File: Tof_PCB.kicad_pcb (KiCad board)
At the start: 2 copper layers, 110.3 x 64.3 mm, 203 parts, among them IC1 NC7WZ00K8X, J1 Screw_Terminal_01x02, J2 Screw_Terminal_01x02, J3 Screw_Terminal_01x02, J4 Conn_02x03_Odd_Even, J5 Conn_01x04, J6 Conn_01x04, M1 mounting_holes_laser, M2 mounting_holes_laser, M3 mounting_holes_laser, M4 mounting_holes_laser, SW1 SW_Push, U1 ATmega328PB-MU, U10 NC7WZ00K8X, U11 UMCC_50Ohm, U12 UMCC_50Ohm, U13 NC7WZ00K8X, U14 NCP81074BDR2G, U15 LMH6559MF, U16 SiPM-MicroRB, U17 UMCC_50Ohm, U18 ts5a4596, U19 ts5a4596, U2 DAC128S085, U20 MAX40658, U21 LP5907MFX-3.3_NOPB, U22 UMCC_50Ohm, U23 TLV3501, U24 TLV3501, U25 HMC589AST89E, U26 UMCC_50Ohm, U27 UMCC_50Ohm, U28 UMCC_50Ohm, U29 UMCC_50Ohm, U3 LM4132BMF, U4 UMCC_50Ohm, U5 UMCC_50Ohm, U6 HMC589AST89E, U7 TLV3501, U8 UMCC_50Ohm, U9 NC7WZ00K8X, Y1 Crystal_GND24

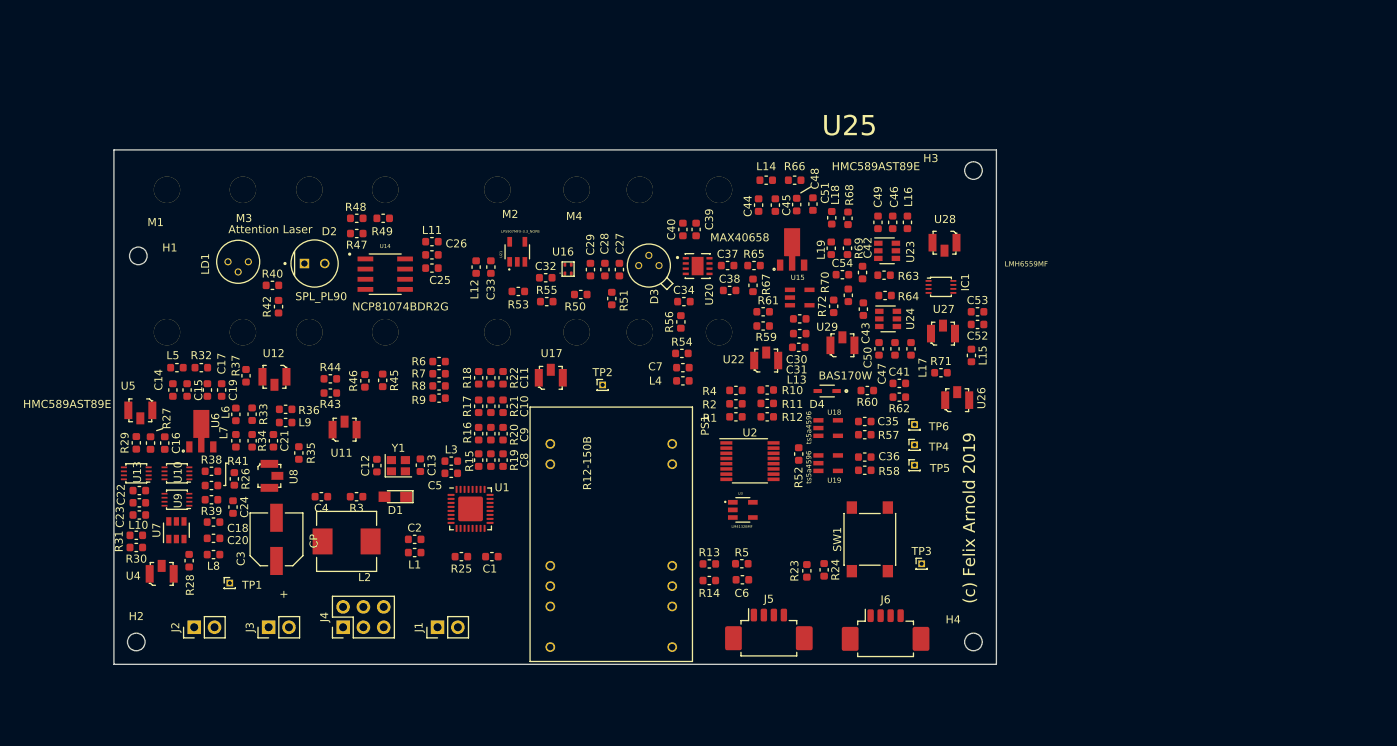
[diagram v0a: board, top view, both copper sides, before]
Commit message: Added RLC values
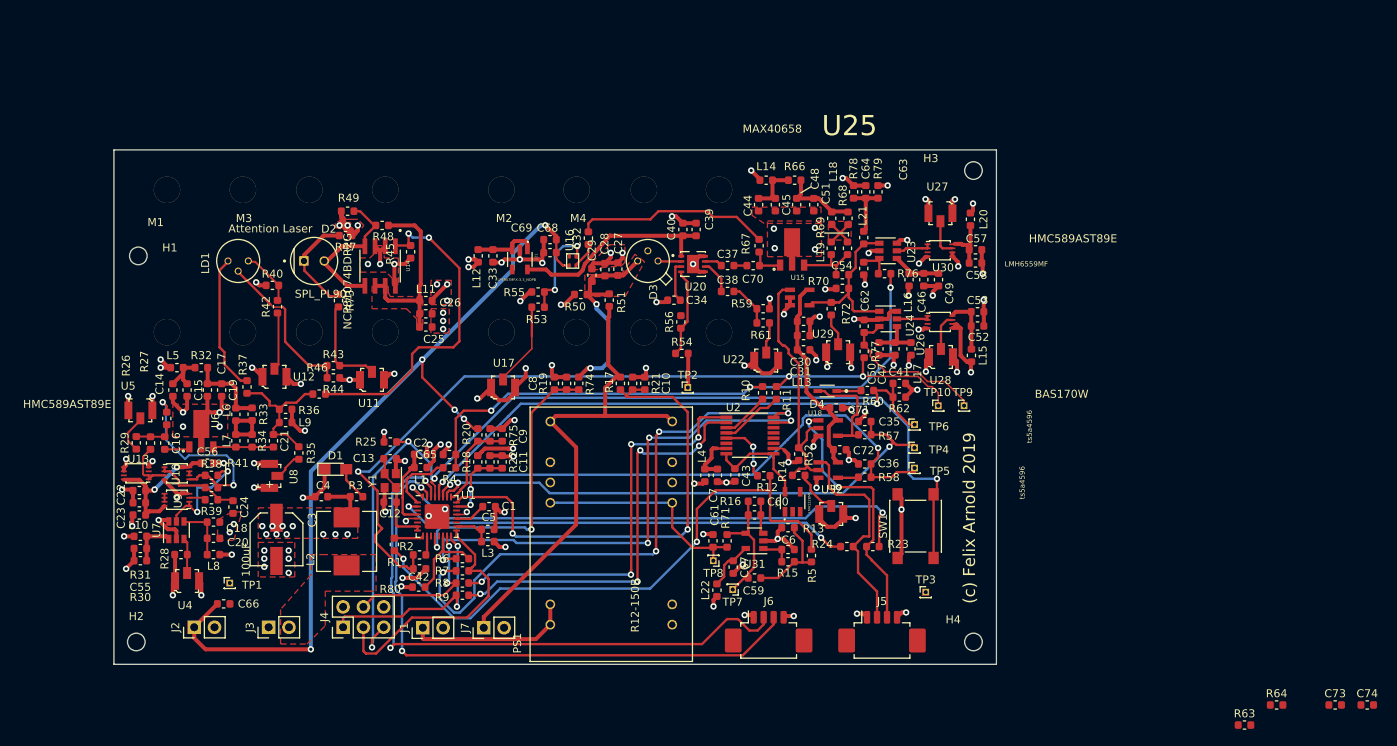
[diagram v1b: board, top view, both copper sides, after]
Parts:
- removed R65: R, Resistor_SMD:R_0603_1608Metric
- added C55: C, Capacitor_SMD:C_0603_1608Metric, F.Cu at (63.0, 99.8)
- added C56: C, Capacitor_SMD:C_0603_1608Metric, F.Cu at (71.4, 89.2)
- added C57: C, Capacitor_SMD:C_0603_1608Metric, F.Cu at (167.4, 62.5)
- added C58: C, Capacitor_SMD:C_0603_1608Metric, F.Cu at (167.4, 64.1)
- added C59: 100nF, Capacitor_SMD:C_0603_1608Metric, F.Cu at (139.8, 103.5)
- added C60: 10nF, Capacitor_SMD:C_0603_1608Metric, F.Cu at (139.8, 95.6)
- added C61: 100nF, Capacitor_SMD:C_0603_1608Metric, F.Cu at (134.6, 98.9)
- added C62: 100nF, Capacitor_SMD:C_0603_1608Metric, F.Cu at (153.5, 72.0)
- added C63: 100nF, Capacitor_SMD:C_0603_1608Metric, F.Cu at (153.4, 64.8)
- added C64: C, Capacitor_SMD:C_0603_1608Metric, F.Cu at (153.7, 55.2)
- added C65: 2.2uF, Capacitor_SMD:C_0603_1608Metric, F.Cu at (101.6, 88.1)
- added C66: 2.2uF, Capacitor_SMD:C_0603_1608Metric, F.Cu at (73.4, 106.7)
- added C67: 100nF, Capacitor_SMD:C_0603_1608Metric, F.Cu at (137.1, 102.1)
- added C68: 2.2uF, Capacitor_SMD:C_0603_1608Metric, F.Cu at (114.2, 61.2)
- added C69: 100nF, Capacitor_SMD:C_0603_1608Metric, F.Cu at (114.2, 62.8)
- added C70: C, Capacitor_SMD:C_0603_1608Metric, F.Cu at (139.6, 64.5)
- added C71: 2.2uF, Capacitor_SMD:C_0603_1608Metric, F.Cu at (150.0, 82.2)
- added C72: 100nF, Capacitor_SMD:C_0603_1608Metric, F.Cu at (150.4, 87.5)
- added C73: 2.2uF, Capacitor_SMD:C_0603_1608Metric, F.Cu at (212.3, 119.4)
- added C74: 2.2uF, Capacitor_SMD:C_0603_1608Metric, F.Cu at (216.4, 119.4)
- added J7: Screw_Terminal_01x02, IODA_Lib:ScrewTerminal_1x02_P2.54mm_Vertical, F.Cu at (105.9, 109.7)
- added L20: L, Inductor_SMD:L_0603_1608Metric, F.Cu at (166.8, 58.7)
- added L21: L, Inductor_SMD:L_0603_1608Metric, F.Cu at (153.4, 61.0)
- added L22: L, Inductor_SMD:L_0603_1608Metric, F.Cu at (135.1, 105.0)
- added R73: R, Resistor_SMD:R_0603_1608Metric, F.Cu at (87.8, 68.8)
- added R74: 1M, Resistor_SMD:R_0603_1608Metric, F.Cu at (117.8, 79.2)
- added R75: 100k, Resistor_SMD:R_0603_1608Metric, F.Cu at (105.2, 85.6)
- added R76: 50k, Resistor_SMD:R_0603_1608Metric, F.Cu at (156.0, 65.5)
- added R77: 50k, Resistor_SMD:R_0603_1608Metric, F.Cu at (153.5, 75.2)
- added R78: R, Resistor_SMD:R_0603_1608Metric, F.Cu at (152.1, 55.2)
- added R79: R, Resistor_SMD:R_0603_1608Metric, F.Cu at (155.2, 55.2)
- added R80: 20k, Resistor_SMD:R_0603_1608Metric, F.Cu at (97.8, 104.6)
- added TP10: TestPoint, Connector_PinHeader_1.00mm:PinHeader_1x01_P1.00mm_Vertical, F.Cu at (162.7, 82.0)
- added TP7: TestPoint, Connector_PinHeader_1.00mm:PinHeader_1x01_P1.00mm_Vertical, F.Cu at (137.0, 105.0)
- added TP8: TestPoint, Connector_PinHeader_1.00mm:PinHeader_1x01_P1.00mm_Vertical, F.Cu at (134.6, 101.3)
- added TP9: TestPoint, Connector_PinHeader_1.00mm:PinHeader_1x01_P1.00mm_Vertical, F.Cu at (166.0, 82.0)
- added U31: LM321, Package_TO_SOT_SMD:SOT-23-5, F.Cu at (139.8, 98.9)
- added U32: UMCC_50Ohm, IODA_Lib:Molex_734120114_UMC_RF_CONN_Vertical, F.Cu at (149.4, 95.5)
- C1, C2, C5, C7: value 100n -> 100nF
- C10, C11, C27, C31, C32, C33, C37, C38, C39, C4, C42, C8, C9: value C -> 2.2uF
- C12, C13: value C -> 16pF
- C28, C29, C30, C40, C43, C6: value C -> 100nF
- C3: value CP -> 100uF
- C34: value C -> 1uF
- L2: value L -> 6.6u
- R1, R10, R11, R12, R23, R24, R50, R6, R7, R8, R9: value R -> 0R
- R13: value R -> 2k
- R14, R55, R61: value R -> 200R
- R15, R18, R19, R20, R21, R22, R5, R54, R56, R71: value R -> 10k
- R16: value R -> 10R
- R17, R51: value R -> 1M
- R2, R4: value R -> 2.2k
- R25: value R -> 20k
- R52, R53: value R -> 50R
- R59, R63: value R -> 75R
- R64: value R -> 150R
- U26: value UMCC_50Ohm -> NC7WZ00K8X; footprint IODA_Lib:Molex_734120114_UMC_RF_CONN_Vertical -> IODA_Lib:VSSOP-8_2.4x2.1mm_P0.5mm
- moved R63 72.1 mm to (201.0, 121.9)
- moved R64 70.8 mm to (205.0, 119.4)
- moved C42 66.6 mm to (97.9, 102.4), turned to 0 degrees
- moved R1 45.6 mm to (94.7, 99.3), turned to 90 degrees
- moved R2 43.8 mm to (97.9, 100.6), turned to 0 degrees
- moved R15 40.7 mm to (144.0, 101.5), turned to 0 degrees
- moved R4 37.1 mm to (101.6, 89.7)
- moved R16 35.5 mm to (139.8, 93.9), turned to 0 degrees
- moved R71 34.0 mm to (136.3, 98.9), turned to 90 degrees
- moved C43 26.2 mm to (137.3, 90.6), turned to 270 degrees
- moved R6 24.8 mm to (103.3, 101.1)
- moved R7 24.8 mm to (103.3, 102.6)
- moved R8 24.8 mm to (103.3, 104.1)
- moved R9 24.8 mm to (103.3, 105.7)
- moved C10 17.9 mm to (126.0, 79.2)
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- renumbered IC1 to U30
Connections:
- net Net-(C25-Pad1) renamed /Tof Tx/ld_driver_supply
- net Net-(R43-Pad1) renamed /Tof Tx/LD_sense
- C42 pad 1: Net-(C42-Pad1) -> /comp_level_2
- C6 pad 1: /V_adj_apd_filt -> GND
- C6 pad 2: GND -> Net-(C6-Pad2)
- J3 pad 1: /5V_in -> GND
- J3 pad 2: GND -> /5V_in
- J5 pad 2: /lockin_2_mc -> /lockin_2
- J5 pad 3: /lockin_1_mc -> /lockin_1
- PS1 pad 17: Net-(PS1-Pad17) -> /V_adj_apd_filt
- PS1 pad 8: Net-(PS1-Pad17) -> /V_adj_apd_filt
- R13 pad 2: Net-(PS1-Pad17) -> Net-(C59-Pad2)
- R14 pad 1: /V_adj_apd_filt -> Net-(R14-Pad1)
- R14 pad 2: Net-(PS1-Pad17) -> Net-(R14-Pad2)
- R15 pad 1: /V_APD_R_SENS -> Net-(C6-Pad2)
- R15 pad 2: /V_APD_R -> Net-(C59-Pad2)
- R16 pad 1: /V_SiPM_SENSE -> Net-(C59-Pad1)
- R16 pad 2: /V_SiPM -> Net-(C60-Pad2)
- R45 pad 2: /Tof Tx/tx_amp_out -> /Tof Tx/ld_driver_in
- R46 pad 1: Net-(R46-Pad1) -> /Tof Tx/tx_amp_out
- R46 pad 2: /Tof Tx/tx_amp_out -> /Tof Tx/ld_driver_in
- R5 pad 1: /V_adj_apd_filt -> Net-(C59-Pad2)
- R52 pad 2: Net-(R52-Pad2) -> Net-(R14-Pad1)
- R63 pad 1: Net-(C42-Pad1) -> Net-(C38-Pad2)
- R63 pad 2: /comp_level_1 -> GND
- R64 pad 1: Net-(C43-Pad1) -> /Tof Rx/TIA_out
- R64 pad 2: /comp_level_2 -> GND
- R71 pad 1: /Tof Rx/rfamp_out -> /V_adj_apd_filt
- R71 pad 2: Net-(R71-Pad2) -> Net-(C59-Pad1)
- U14 pad 1: Net-(R46-Pad1) -> /Tof Tx/ld_driver_in
- U15 pad 1: Net-(R52-Pad2) -> Net-(R14-Pad1)
- U18 pad 2: Net-(R52-Pad2) -> Net-(R14-Pad1)
- U19 pad 2: Net-(R52-Pad2) -> Net-(R14-Pad1)
- U2 pad 8: Net-(U2-Pad8) -> Net-(C43-Pad1)
- U2 pad 9: Net-(U2-Pad8) -> Net-(C43-Pad1)
- U23 pad 3: Net-(C42-Pad1) -> Net-(C63-Pad1)
- U24 pad 3: Net-(C43-Pad1) -> Net-(C62-Pad1)
- U24 pad 5: Net-(IC1-Pad5) -> Net-(U24-Pad5)
- U26 pad 1: GND -> Net-(U24-Pad5)
- U26 pad 2: Net-(R71-Pad2) -> Net-(U24-Pad5)
- U26 pad 3: GND -> Net-(U26-Pad3)
- U28 pad 2: Net-(IC1-Pad3) -> Net-(U26-Pad7)
- U3 pad 5: Net-(U2-Pad8) -> Net-(C43-Pad1)
- U30 pad 3: Net-(IC1-Pad3) -> Net-(U30-Pad3)
- U30 pad 5: Net-(IC1-Pad5) -> +5V
- U30 pad 6: Net-(IC1-Pad5) -> +5V
- U30 pad 8: Net-(C52-Pad1) -> Net-(C57-Pad1)
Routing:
- net GND: track 0.00 -> 265.8 mm, vias 0 -> 108
- net /~reset: track 0.00 -> 126.4 mm, vias 0 -> 4
- net /V_SiPM: track 0.00 -> 104.7 mm, vias 0 -> 5
- net /comp_level_2: track 0.00 -> 102.7 mm, vias 0 -> 3
- net /RXD: track 0.00 -> 77.1 mm, vias 0 -> 2
- net /comp_level_1: track 0.00 -> 75.6 mm, vias 0 -> 3
- net /TXD: track 0.00 -> 74.7 mm, vias 0 -> 2
- net /V_adj_apd: track 0.00 -> 73.4 mm, vias 0 -> 2
- net /lockin_1_peak: track 0.00 -> 71.7 mm, vias 0 -> 2
- net /lockin_2_filt: track 0.00 -> 71.7 mm, vias 0 -> 2
- net Net-(R7-Pad1): track 0.00 -> 71.6 mm, vias 0 -> 4
- net /lockin_1_filt: track 0.00 -> 68.4 mm, vias 0 -> 2
- net /lockin_1_mc: track 0.00 -> 67.5 mm, vias 0 -> 2
- net Net-(R6-Pad1): track 0.00 -> 64.4 mm, vias 0 -> 4
- net /V_APD: track 0.00 -> 63.2 mm
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- added copper zone on F.Cu, net +5V
- added copper zone on In2.Cu, net +5V
- added copper zone on F.Cu, net /5V_in
- added copper zone on F.Cu, net /Tof Tx/ld_driver_supply
- added copper zone on F.Cu, net /V_APD_R
- added copper zone on F.Cu, net GND
- added copper zone on In1.Cu, net GND
- added copper zone on F.Cu, net Net-(L18-Pad2)
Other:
- copper layers 2 -> 4
- net class 50Ohms added: clearance 0.2, trace_width 0.3048, via_dia 0.8, via_drill 0.4
- net class Default: trace_width 0.25 -> 0.3
- net class Power added: clearance 0.2, trace_width 0.5, via_dia 0.8, via_drill 0.4

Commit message: Added more digikey numbers in BOM
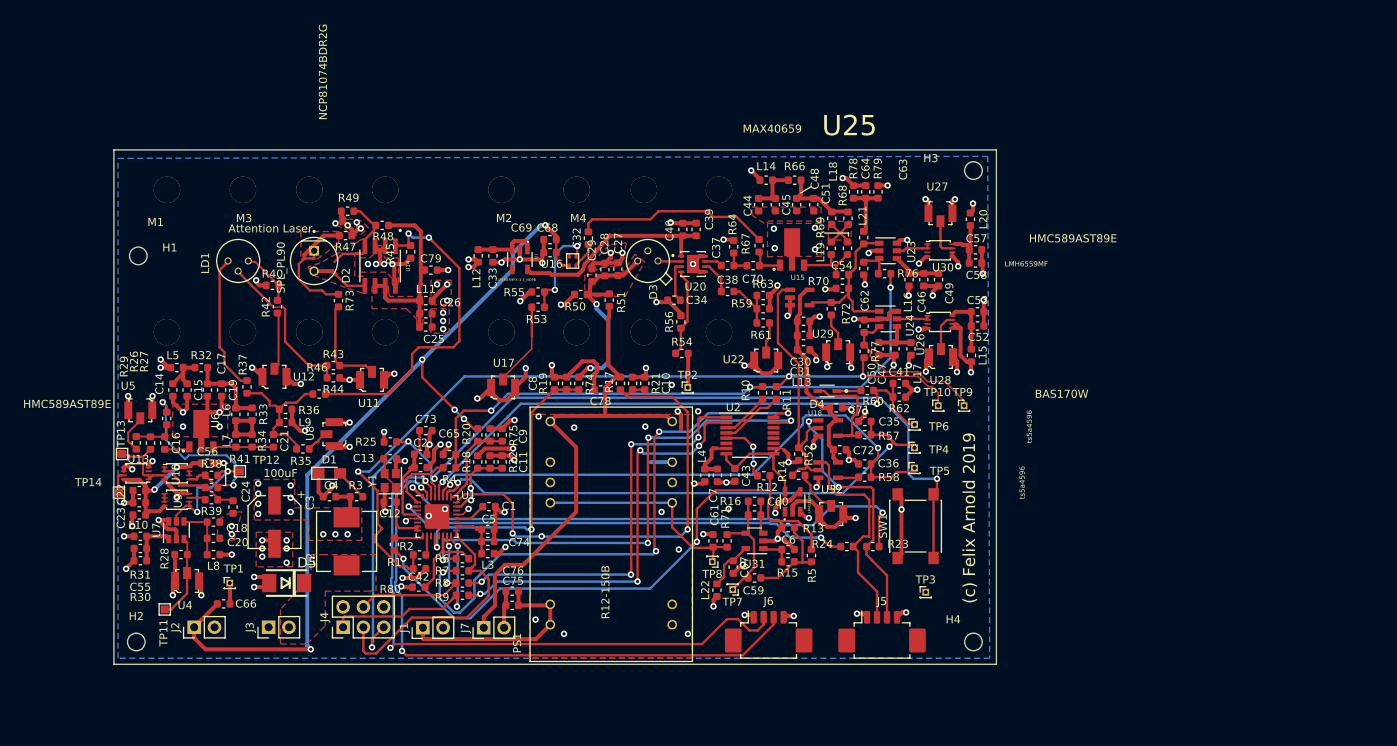
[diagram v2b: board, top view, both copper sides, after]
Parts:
- added C75: 2.2uF, Capacitor_SMD:C_0603_1608Metric, F.Cu at (109.5, 106.9)
- added C76: 2.2uF, Capacitor_SMD:C_0603_1608Metric, F.Cu at (109.5, 105.2)
- added C78: 10nF, 250V, Capacitor_SMD:C_0603_1608Metric, F.Cu at (120.5, 80.0)
- added C79: 2.2uF, Capacitor_SMD:C_0603_1608Metric, F.Cu at (99.3, 65.0)
- added D5: SMBJ6.0A, OLIMEX_Diodes-FP:DO214AA_1(K)-2(A), F.Cu at (81.3, 104.1)
- added TP11: TestPoint, TestPoint:TestPoint_Pad_1.0x1.0mm, F.Cu at (66.0, 107.4)
- added TP12: TestPoint, TestPoint:TestPoint_Pad_1.0x1.0mm, F.Cu at (75.4, 90.2)
- added TP13: TestPoint, TestPoint:TestPoint_Pad_1.0x1.0mm, F.Cu at (60.7, 88.0)
- added TP14: TestPoint, TestPoint:TestPoint_Pad_1.0x1.0mm, F.Cu at (60.3, 92.8)
- C14, C16, C17, C20, C21, C22, C24, C25, C35, C36, C41, C44, C48, C49, C50, C52, C54, C55, C57, C70: value C -> 2.2uF
- C15, C18, C19, C23, C26, C45, C46, C47, C51, C53, C56, C58, C64: value C -> 100nF
- C27: value 2.2uF -> 10nF, 250V
- C28, C29: value 100nF -> 10nF, 250V
- C60: value 10nF -> 100nF
- L18, L19, L21, L6, L7, L9: value L -> 10uH
- R13: value 2k -> 2.2k
- R16: value 10R -> 100R
- R26, R27, R37, R38, R39, R41, R46, R67: value R -> 0R
- R28, R36, R45, R70: value R -> 50R
- R29, R35, R42, R43, R72, R73, R78, R79: value R -> 200R
- R30, R31: value R -> 1k
- R32, R66: value R -> 1.8R
- R33, R34, R57, R58, R60, R68, R69: value R -> 10k
- R40, R44: value R -> 100R
- R47: value R -> 5R
- R48, R49: value R -> open
- R62: value R -> 100k
- U20: value MAX40658 -> MAX40659
- moved C73 118.7 mm to (98.7, 85.1)
- moved C74 111.8 mm to (106.4, 98.9)
- moved R64 88.8 mm to (137.2, 62.1), turned to 90 degrees
- moved R63 80.6 mm to (140.8, 68.2)
- moved U8 9.65 mm to (87.2, 85.5), turned to 90 degrees
- moved C3 2.17 mm to (79.8, 96.5)
- moved L3 1.50 mm to (106.4, 100.5)
- moved C4 1.02 mm to (86.6, 93.3)
- moved D1 0.92 mm to (86.6, 90.4)
- moved R35 0.72 mm to (83.3, 87.4), turned to 180 degrees
- moved TP8 0.18 mm to (134.5, 101.5)
- turned D2 to 270 degrees
- turned U16 to 90 degrees
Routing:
- net GND: track 265.8 -> 305.6 mm, vias 108 -> 126
- net /Tof Tx/start: track 4.43 -> 10.6 mm
- net /12V_in: track 20.6 -> 26.4 mm
- net +5V: track 56.6 -> 62.3 mm, vias 37 -> 39
- net Net-(D2-Pad1): track 12.5 -> 16.6 mm
- net Net-(C2-Pad1): track 10.2 -> 13.4 mm
- net /Tof Tx/start_pulse_inv: track 6.94 -> 9.66 mm
- net /Tof Tx/start_pulse: track 0.00 -> 2.58 mm
- net Net-(C38-Pad2): track 5.54 -> 7.19 mm
- net /Tof Rx/TIA_out: track 1.73 -> 3.30 mm
- net /Tof Tx/start_th: track 13.8 -> 15.4 mm
- net Net-(C5-Pad1): track 4.80 -> 6.32 mm
- net /V_APD: track 63.2 -> 64.6 mm
- net /lockin_1_mc: track 67.5 -> 68.2 mm
- net Net-(R35-Pad1): track 3.69 -> 3.06 mm
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- added copper zone on B.Cu, net GND
- added copper zone on F.Cu, net Net-(D2-Pad1)
- added copper zone on F.Cu, net Net-(D2-Pad2)

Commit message: solved drc errors
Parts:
- added R65: 0R, Resistor_SMD:R_0603_1608Metric, F.Cu at (60.0, 56.1)
- added R81: 0R, Resistor_SMD:R_0603_1608Metric, F.Cu at (162.6, 53.2)
- added R82: 0R, Resistor_SMD:R_0603_1608Metric, F.Cu at (60.3, 107.8)
- added R83: 0R, Resistor_SMD:R_0603_1608Metric, F.Cu at (163.9, 111.0)
- D1: footprint LEDs:LED_0805_HandSoldering -> LEDs:LED_0805
- L2: value 6.6u -> 6.8u
- moved H1 12.0 mm to (57.5, 52.5)
- moved H2 4.98 mm to (57.5, 111.5)
- moved C66 1.87 mm to (73.1, 104.9)
- moved C75 1.83 mm to (109.5, 105.1)
- moved C76 1.83 mm to (109.5, 103.3)
- moved TP1 1.14 mm to (74.2, 103.0)
- moved H3 0.38 mm to (167.5, 52.5)
- moved H4 0.37 mm to (167.5, 111.5)
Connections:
- net Net-(R14-Pad1) renamed /Tof Rx/buffer_out
- C13 pad 1: /XTAL1 -> /XTAL2
- H1 pad 1: GND -> Net-(H1-Pad1)
- H2 pad 1: GND -> Net-(H2-Pad1)
- H3 pad 1: GND -> Net-(H3-Pad1)
- H4 pad 1: GND -> Net-(H4-Pad1)
- PS1 pad 9: Net-(PS1-Pad16) -> Net-(PS1-Pad9)
- U1 pad 8: /XTAL1 -> /XTAL2
- Y1 pad 3: /XTAL1 -> /XTAL2
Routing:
- net /XTAL2: track 0.00 -> 16.3 mm
- net GND: track 305.6 -> 312.8 mm, vias 126 -> 130
- net /XTAL1: track 12.4 -> 7.67 mm
- net Net-(H2-Pad1): track 0.00 -> 4.48 mm
- net Net-(H3-Pad1): track 0.00 -> 4.40 mm
- net Net-(H1-Pad1): track 0.00 -> 4.34 mm
- net Net-(H4-Pad1): track 0.00 -> 3.78 mm
- net /V_SiPM: track 105.1 -> 107.4 mm
- net /12V_in: track 26.4 -> 28.2 mm
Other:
- board size 110.3 x 64.3 mm -> 115 x 64.3 mm
- net class 50Ohms: trace_width 0.3048 -> 0.36

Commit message: bugfixes
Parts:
- added C77: c_rf_filt, Capacitor_SMD:C_0603_1608Metric, F.Cu at (156.1, 59.9)
- added C80: 2.2uF, Capacitor_SMD:C_0603_1608Metric, F.Cu at (148.8, 103.1)
- added C81: 2.2uF, Capacitor_SMD:C_0603_1608Metric, F.Cu at (151.4, 70.2)
- added C82: 100nF, Capacitor_SMD:C_0603_1608Metric, B.Cu at (86.2, 67.0)
- added C83: 2.2uF, Capacitor_SMD:C_0603_1608Metric, B.Cu at (87.8, 67.0)
- added D6: LED, LEDs:LED_0805, F.Cu at (75.8, 58.4)
- added FID1: Fiducial, MF_Aesthetics:MF_Aesthetics-FIDUCIAL_100MIL, F.Cu at (58.2, 65.0)
- added FID2: Fiducial, MF_Aesthetics:MF_Aesthetics-FIDUCIAL_100MIL, F.Cu at (57.6, 104.0)
- added FID3: Fiducial, MF_Aesthetics:MF_Aesthetics-FIDUCIAL_100MIL, F.Cu at (162.8, 105.6)
- added R84: 2.2k, Resistor_SMD:R_0603_1608Metric, F.Cu at (63.0, 102.9)
- added R85: 50R, Resistor_SMD:R_0603_1608Metric, F.Cu at (105.8, 91.6)
- added R86: 200R, Resistor_SMD:R_0603_1608Metric, F.Cu at (75.9, 54.6)
- added R87: 0R, Resistor_SMD:R_0603_1608Metric, F.Cu at (72.1, 95.4)
- added R88: 0R, Resistor_SMD:R_0603_1608Metric, F.Cu at (139.6, 66.4)
- added R89: 22R, Resistor_SMD:R_0603_1608Metric, F.Cu at (161.1, 60.0)
- added R90: 22R, Resistor_SMD:R_0603_1608Metric, F.Cu at (164.3, 60.0)
- added R91: 22R, Resistor_SMD:R_0603_1608Metric, F.Cu at (163.6, 73.7)
- added R92: 10k, Resistor_SMD:R_0603_1608Metric, F.Cu at (157.3, 104.3)
- added R93: 10k, Resistor_SMD:R_0603_1608Metric, F.Cu at (153.3, 104.3)
- added U33: UMCC_50Ohm, IODA_Lib:Molex_734120114_UMC_RF_CONN_Vertical, F.Cu at (108.9, 92.3)
- added U34: NC7WZ16, IODA_Lib:SOT65P210X110-6N, F.Cu at (67.5, 96.3)
- added U35: UMCC_50Ohm, IODA_Lib:Molex_734120114_UMC_RF_CONN_Vertical, F.Cu at (158.8, 56.8)
- C24: value 2.2uF -> c_tx_filt
- C34: value 1uF -> 2.2uF
- L1, L10, L11, L12, L13, L14, L15, L16, L17, L20, L22, L3, L4, L5, L8: value L -> bead
- R25, R80: value 20k -> 10k
- R3, R30, R31: value 1k -> 2.2k
- R47: value 5R -> 4.7R
- R64: value 150R -> 22R
- R76, R77: value 50k -> 100k
- moved TP3 13.1 mm to (165.8, 93.0)
- moved R63 9.77 mm to (134.8, 60.5), turned to 90 degrees
- moved C79 8.09 mm to (91.5, 67.1), turned to 90 degrees
- moved R73 5.98 mm to (81.8, 68.3), turned to 0 degrees
- moved L11 5.96 mm to (94.1, 72.6)
- moved C25 5.47 mm to (94.0, 69.3)
- moved R45 5.21 mm to (91.6, 63.3)
- moved R47 5.21 mm to (83.5, 61.2)
- moved R48 5.21 mm to (88.0, 60.0)
- moved U14 5.21 mm to (87.8, 65.0)
- moved D2 5.11 mm to (79.6, 63.9)
- moved M3 5.11 mm to (79.6, 63.9)
- moved C26 4.71 mm to (94.0, 70.9)
- moved R42 4.13 mm to (76.0, 70.0)
- moved TP4 3.81 mm to (163.6, 87.0)
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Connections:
- net /Tof Tx/pulsegen_bypass renamed /Tof Tx/pg_bypass
- net /Tof Tx/start_pulse_inv renamed /Tof Tx/pulse_inv
- net Net-(C18-Pad1) renamed /Tof Tx/supply_th
- C37 pad 2: /Tof Rx/TIA_out -> Net-(C37-Pad2)
- C38 pad 2: Net-(C38-Pad2) -> /Tof Rx/con
- R38 pad 2: /Tof Tx/start_th -> Net-(R38-Pad2)
- R59 pad 1: Net-(C38-Pad2) -> /Tof Rx/con
- R61 pad 2: Net-(C38-Pad2) -> /Tof Rx/con
- R63 pad 1: Net-(C38-Pad2) -> Net-(C37-Pad2)
- R64 pad 2: GND -> Net-(C37-Pad2)
- R67 pad 2: Net-(C70-Pad2) -> /Tof Rx/TIA_out
- R70 pad 2: /Tof Rx/rfamp_out -> Net-(C81-Pad1)
- R72 pad 1: /Tof Rx/rfamp_out -> Net-(C81-Pad1)
- TP12 pad 1: /Tof Tx/start_th -> Net-(R38-Pad2)
- U1 pad 22: Net-(U1-Pad22) -> /stop_mc
- U1 pad 6: Net-(U1-Pad6) -> /start_mc
- U26 pad 7: Net-(U26-Pad7) -> Net-(R91-Pad2)
- U27 pad 2: Net-(U27-Pad2) -> Net-(R90-Pad1)
- U28 pad 2: Net-(U26-Pad7) -> Net-(R91-Pad1)
- U30 pad 5: +5V -> Net-(R90-Pad2)
- U30 pad 6: +5V -> Net-(R90-Pad2)
- U30 pad 7: Net-(U27-Pad2) -> Net-(R90-Pad2)
- U9 pad 1: /Tof Tx/start_th -> Net-(R38-Pad2)
- U9 pad 2: /Tof Tx/start_th -> Net-(R38-Pad2)
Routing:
- net /start_mc: track 0.00 -> 34.3 mm, vias 0 -> 4
- net GND: track 312.8 -> 342.9 mm, vias 130 -> 139
- net /Tof Tx/ld_driver_supply: track 24.0 -> 46.3 mm, vias 0 -> 2
- net Net-(R38-Pad2): track 0.00 -> 17.0 mm, vias 0 -> 2
- net /stop_mc: track 0.00 -> 9.29 mm, vias 0 -> 2
- net /Tof Rx/con: track 0.00 -> 9.08 mm
- net /Tof Tx/start_th: track 15.4 -> 7.01 mm, vias 2 -> 0
- net Net-(C38-Pad2): track 7.19 -> 0.00 mm
- net Net-(R90-Pad2): track 0.00 -> 5.09 mm
- net /Tof Tx/ld_driver_in: track 41.5 -> 36.5 mm
- net Net-(U27-Pad2): track 4.72 -> 0.00 mm
- net Net-(U26-Pad7): track 4.62 -> 0.00 mm
- net Net-(C81-Pad1): track 0.00 -> 4.34 mm
- net Net-(C37-Pad2): track 0.00 -> 4.14 mm
- net /lockin_1_filt: track 68.8 -> 72.6 mm
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- added copper zone on F.Cu, net /Tof Rx/3V3
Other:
- board size 115 x 64.3 mm -> 115 x 65 mm
- net class High Voltage added: clearance 0.4, trace_width 0.5, via_dia 0.8, via_drill 0.4
- rule pad_to_mask_clearance: 0.051 -> 0
- rule solder_mask_min_width: 0.25 -> 0.15
- board text added: "(c) Felix Arnold 11.11.2019"
- board text added: "Tof Compact"
- board text added: "wires"
- board text removed: "(c) Felix Arnold 2019"
